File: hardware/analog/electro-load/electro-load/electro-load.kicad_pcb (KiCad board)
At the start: 2 copper layers, 178 x 119 mm, 140 parts, among them J1 AVR-ISP-10, J2 Conn_WallSocket_Earth, J3 INPUT, J4 INPUT, K1 SANYOU_SRD_Form_C, M1 Noctua NF-A14 5V, Q1 2N2222A, Q2 2N2222A, Q3 IPP037N06L3, Q4 IPP037N06L3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

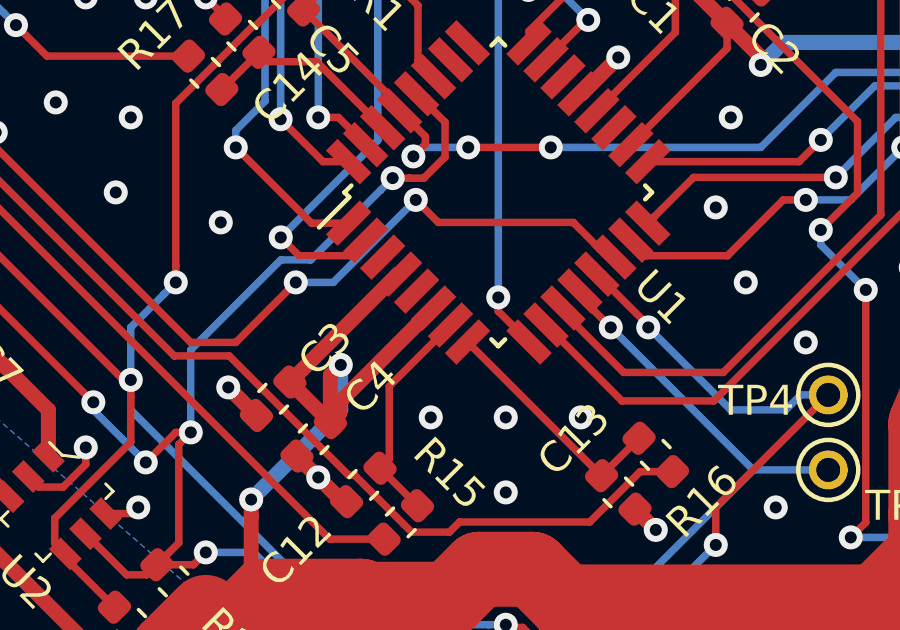
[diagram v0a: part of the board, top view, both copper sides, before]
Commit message: Fixed missing GND trace on SAMD21
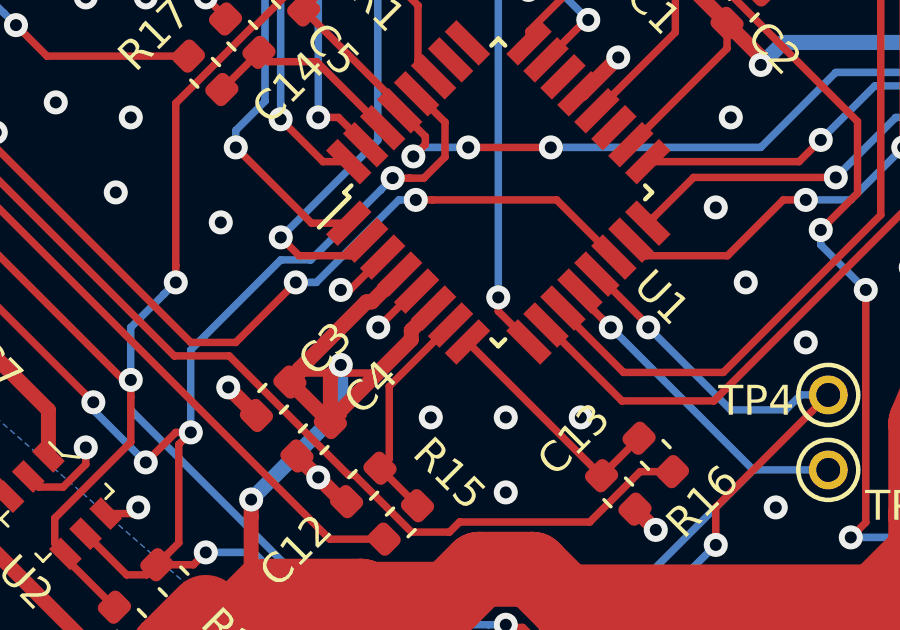
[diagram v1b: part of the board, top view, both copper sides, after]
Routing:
- net GND: track 60.5 -> 64.1 mm, vias 494 -> 496
- net +5V: track 738.6 -> 736.1 mm
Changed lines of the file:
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@@
     (thickness 1.6)
     (drawings 48)
-    (tracks 2043)
+    (tracks 2053)
     (zones 0)
     (modules 140)
@@
     (solder_mask_min_width 0.25)
     (aux_axis_origin 0 0)
-    (visible_elements 7FF5FF7F)
+    (visible_elements 7FFDFF7F)
     (pcbplotparams
       (layerselection 0x010fc_ffffffff)
@@
   (via (at 176 87) (size 0.8) (drill 0.4) (layers F.Cu B.Cu) (net 1))
   (via (at 173.5 89.5) (size 0.8) (drill 0.4) (layers F.Cu B.Cu) (net 1))
+  (segment (start 196.961953 50.788047) (end 195.75 52) (width 0.25) (layer F.Cu) (net 1))
+  (segment (start 197.027639 50.788047) (end 196.961953 50.788047) (width 0.25) (layer F.Cu) (net 1))
+  (via (at 195.75 52) (size 0.8) (drill 0.4) (layers F.Cu B.Cu) (net 1))
+  (segment (start 194.802944 50.75) (end 194.5 50.75) (width 0.25) (layer F.Cu) (net 1))
+  (via (at 194.5 50.75) (size 0.8) (drill 0.4) (layers F.Cu B.Cu) (net 1))
+  (segment (start 195.896268 49.656676) (end 194.802944 50.75) (width 0.25) (layer F.Cu) (net 1))
   (segment (start 188.405065 62.103117) (end 189.483403 61.024779) (width 0.2) (layer F.Cu) (net 2))
   (segment (start 188.069189 62.438993) (end 188.405065 62.103117) (width 0.2) (layer F.Cu) (net 2))
@@
   (segment (start 172.3125 109.065354) (end 172.297854 109.08) (width 0.5) (layer F.Cu) (net 2))
   (segment (start 172.3125 106.95) (end 172.3125 109.065354) (width 0.5) (layer F.Cu) (net 2))
-  (segment (start 196.349711 50.222361) (end 196.461953 50.222361) (width 0.25) (layer F.Cu) (net 2))
-  (segment (start 193.052803 53.519269) (end 196.349711 50.222361) (width 0.25) (layer F.Cu) (net 2))
-  (segment (start 193.052803 54.071283) (end 193.052803 53.519269) (width 0.25) (layer F.Cu) (net 2))
-  (segment (start 194.403377 54.543679) (end 194.403377 55.421857) (width 0.25) (layer F.Cu) (net 2))
-  (segment (start 197.593324 51.353732) (end 194.403377 54.543679) (width 0.25) (layer F.Cu) (net 2))
-  (segment (start 194.403377 55.421857) (end 193.052803 54.071283) (width 0.25) (layer F.Cu) (net 2))
   (segment (start 205.651881 42.163805) (end 203.038047 44.777639) (width 0.25) (layer F.Cu) (net 2))
   (segment (start 205.651881 40.759262) (end 205.651881 42.163805) (width 0.25) (layer F.Cu) (net 2))
@@
   (segment (start 181.174898 56.181098) (end 181.952716 56.181098) (width 0.5) (layer F.Cu) (net 2))
   (segment (start 188.75 64.25) (end 188.75 62.75) (width 2.5) (layer F.Cu) (net 2))
-  (segment (start 194.462736 54.48432) (end 197.593324 51.353732) (width 0.5) (layer F.Cu) (net 2))
-  (segment (start 194.462736 54.862498) (end 194.462736 54.48432) (width 0.5) (layer F.Cu) (net 2))
-  (segment (start 194.153377 55.171857) (end 194.462736 54.862498) (width 0.5) (layer F.Cu) (net 2))
-  (segment (start 196.401725 50.222361) (end 192.802803 53.821283) (width 0.5) (layer F.Cu) (net 2))
-  (segment (start 196.461953 50.222361) (end 196.401725 50.222361) (width 0.5) (layer F.Cu) (net 2))
   (segment (start 194.153377 55.171857) (end 192.802803 53.821283) (width 0.5) (layer F.Cu) (net 2))
   (via (at 194.5 53.25) (size 0.8) (drill 0.4) (layers F.Cu B.Cu) (net 2))
@@
   (segment (start 194.5 82.46) (end 197.55 79.41) (width 0.5) (layer F.Cu) (net 2))
   (segment (start 197.55 79.41) (end 198.6275 79.41) (width 0.5) (layer F.Cu) (net 2))
+  (segment (start 196.850002 52.097054) (end 197.593324 51.353732) (width 0.5) (layer F.Cu) (net 2))
+  (segment (start 197.593324 51.47968) (end 195.553735 53.519269) (width 0.25) (layer F.Cu) (net 2))
+  (segment (start 197.593324 51.353732) (end 197.593324 51.47968) (width 0.25) (layer F.Cu) (net 2))
+  (segment (start 195.553735 53.519269) (end 193.165045 53.519269) (width 0.25) (layer F.Cu) (net 2))
+  (segment (start 194.462736 54.795268) (end 196.850002 52.408002) (width 0.5) (layer F.Cu) (net 2))
+  (segment (start 194.462736 54.862498) (end 194.462736 54.795268) (width 0.5) (layer F.Cu) (net 2))
+  (segment (start 193.165045 53.519269) (end 196.461953 50.222361) (width 0.25) (layer F.Cu) (net 2))
+  (segment (start 196.850002 52.408002) (end 196.850002 52.097054) (width 0.5) (layer F.Cu) (net 2))
+  (segment (start 194.153377 55.171857) (end 194.462736 54.862498) (width 0.5) (layer F.Cu) (net 2))
+  (segment (start 195.350002 51.149998) (end 193.112162 53.387838) (width 0.5) (layer F.Cu) (net 2))
+  (segment (start 193.112162 53.387838) (end 193.112162 53.511924) (width 0.5) (layer F.Cu) (net 2))
+  (segment (start 195.534316 51.149998) (end 195.350002 51.149998) (width 0.5) (layer F.Cu) (net 2))
+  (segment (start 196.461953 50.222361) (end 195.534316 51.149998) (width 0.5) (layer F.Cu) (net 2))
+  (segment (start 193.112162 53.511924) (end 192.802803 53.821283) (width 0.5) (layer F.Cu) (net 2))
   (segment (start 193.60057 41.082554) (end 194.678908 40.004216) (width 0.2) (layer F.Cu) (net 3))
   (segment (start 193.264694 41.41843) (end 193.60057 41.082554) (width 0.2) (layer F.Cu) (net 3))
@@
   (segment (start 119.75 39.8375) (end 119.5 39.5875) (width 0.2) (layer F.Cu) (net 19))
   (segment (start 119.75 43.55) (end 119.75 39.8375) (width 0.2) (layer F.Cu) (net 19))
-  (segment (start 194.25 50.5) (end 193 50.5) (width 0.25) (layer B.Cu) (net 19))
-  (segment (start 203.603732 49.656676) (end 203.406676 49.656676) (width 0.25) (layer F.Cu) (net 19))
-  (segment (start 197.75 48.5) (end 197 47.75) (width 0.25) (layer F.Cu) (net 19))
-  (segment (start 203.406676 49.656676) (end 202.25 48.5) (width 0.25) (layer F.Cu) (net 19))
-  (segment (start 202.25 48.5) (end 197.75 48.5) (width 0.25) (layer F.Cu) (net 19))
-  (segment (start 197 47.75) (end 194.25 50.5) (width 0.25) (layer B.Cu) (net 19))
   (via (at 193 50.5) (size 0.8) (drill 0.4) (layers F.Cu B.Cu) (net 19))
   (via (at 197 47.75) (size 0.8) (drill 0.4) (layers F.Cu B.Cu) (net 19))
@@
   (segment (start 183 46) (end 183 45.5) (width 0.25) (layer F.Cu) (net 19))
   (segment (start 189.5 52.5) (end 183 46) (width 0.25) (layer F.Cu) (net 19))
+  (segment (start 203.603732 49.656676) (end 201.697056 47.75) (width 0.25) (layer F.Cu) (net 19))
+  (segment (start 197 47.75) (end 196.434315 47.75) (width 0.25) (layer B.Cu) (net 19))
+  (segment (start 201.697056 47.75) (end 197.565685 47.75) (width 0.25) (layer F.Cu) (net 19))
+  (segment (start 193.684315 50.5) (end 193.565685 50.5) (width 0.25) (layer B.Cu) (net 19))
+  (segment (start 197.565685 47.75) (end 197 47.75) (width 0.25) (layer F.Cu) (net 19))
+  (segment (start 196.434315 47.75) (end 193.684315 50.5) (width 0.25) (layer B.Cu) (net 19))
+  (segment (start 193.565685 50.5) (end 193 50.5) (width 0.25) (layer B.Cu) (net 19))
   (via (at 118.75 48.5) (size 0.8) (drill 0.4) (layers F.Cu B.Cu) (net 20))
   (via (at 114.25 48.25) (size 0.8) (drill 0.4) (layers F.Cu B.Cu) (net 20))

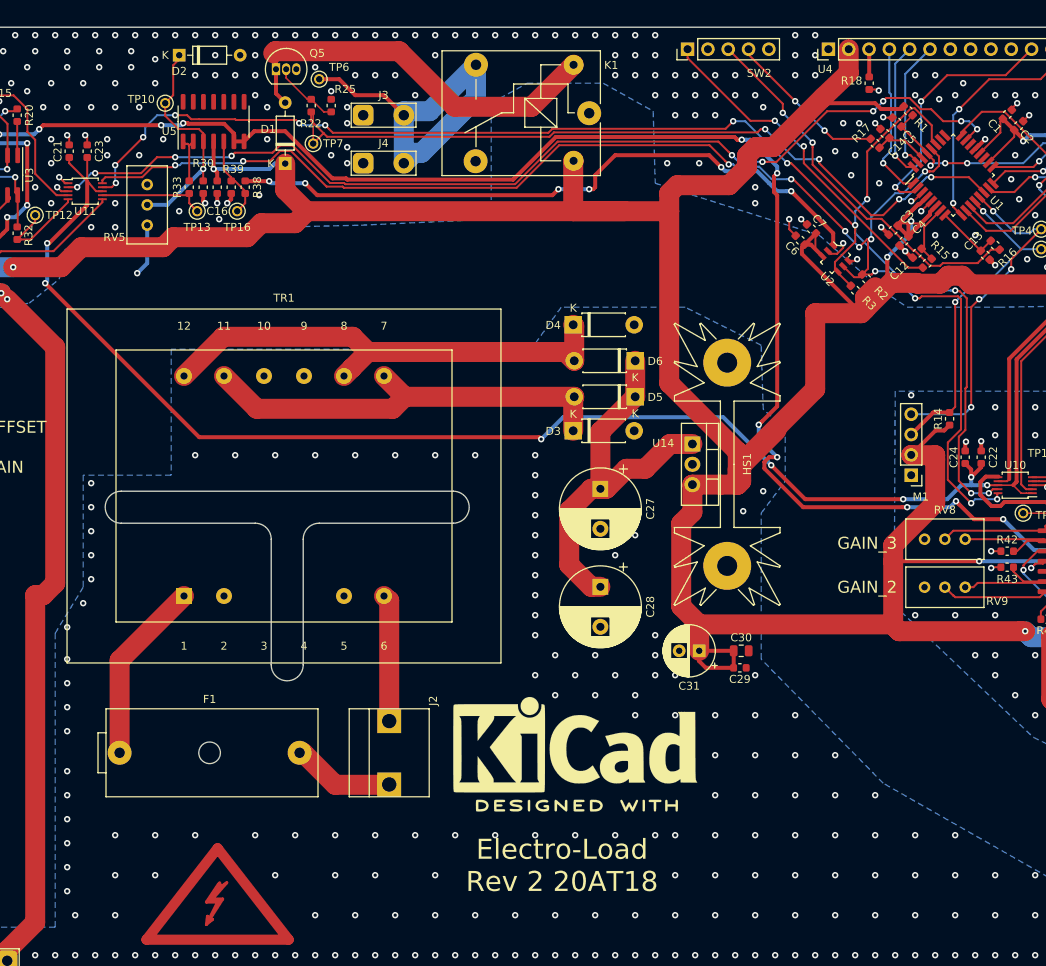
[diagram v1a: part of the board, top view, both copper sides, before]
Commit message: Added mounting holes and added silkscreen text for V_DIV
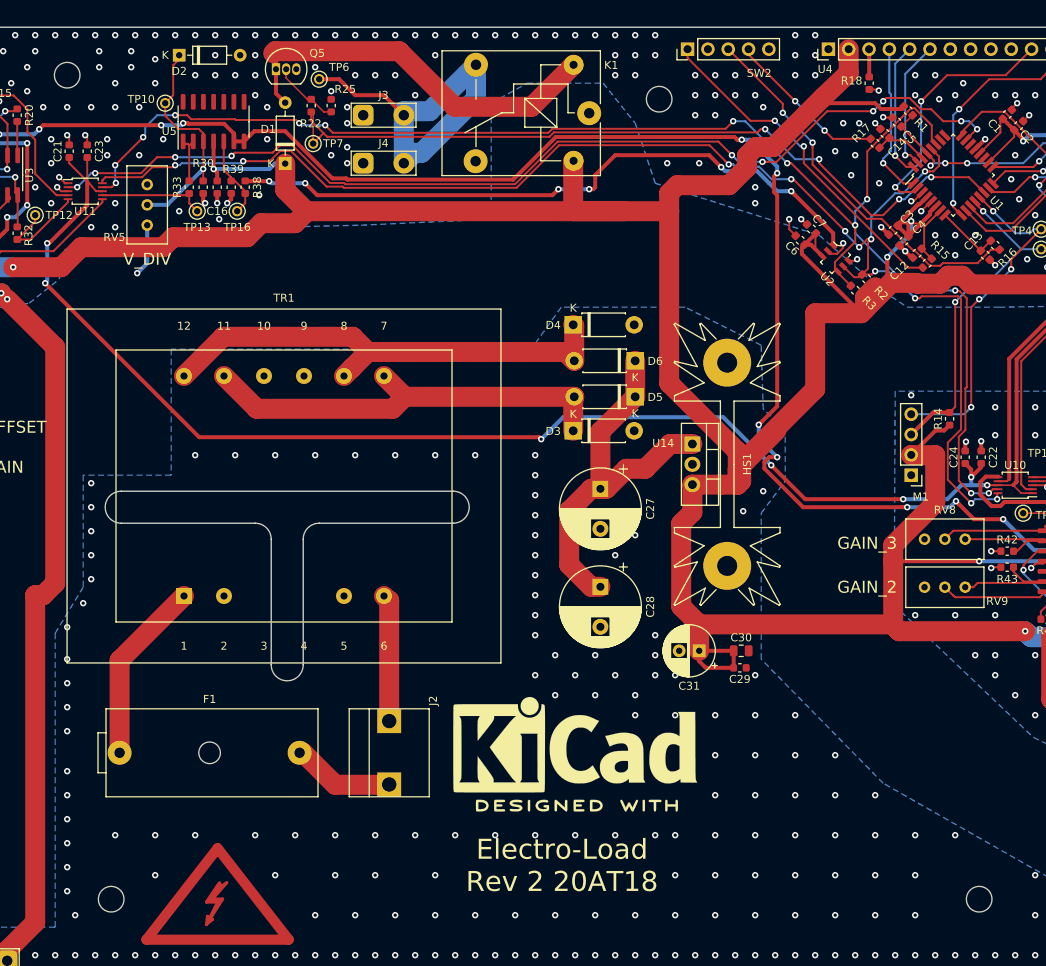
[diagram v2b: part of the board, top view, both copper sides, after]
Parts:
- added REF**: MountingHole_3.2mm_M3, MountingHole:MountingHole_3.2mm_M3, F.Cu at (89.0, 35.0)
- added REF**: MountingHole_3.2mm_M3, MountingHole:MountingHole_3.2mm_M3, F.Cu at (163.0, 38.0)
- added REF**: MountingHole_3.2mm_M3, MountingHole:MountingHole_3.2mm_M3, F.Cu at (203.0, 138.0)
- added REF**: MountingHole_3.2mm_M3, MountingHole:MountingHole_3.2mm_M3, F.Cu at (94.5, 138.0)
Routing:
- net GND: vias 496 -> 481
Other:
- board text added: "V_DIV"
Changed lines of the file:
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@@
   (general
     (thickness 1.6)
-    (drawings 48)
-    (tracks 2053)
+    (drawings 49)
+    (tracks 2038)
     (zones 0)
-    (modules 140)
+    (modules 144)
     (nets 89)
   )
@@
     (add_net "/Current Measurements/LOAD_CURRENT")
   )
+  (module MountingHole:MountingHole_3.2mm_M3 (layer F.Cu)
+    (at 89 35)
+    (descr "Mounting Hole 3.2mm, no annular, M3")
+    (tags "mounting hole 3.2mm no annular m3")
+    (attr virtual)
+    (fp_text reference REF** (at 0 -4.2) (layer F.SilkS) hide
+      (effects (font (size 1 1) (thickness 0.15)))
+    )
+    (fp_text value MountingHole_3.2mm_M3 (at 0 4.2) (layer F.Fab)
+      (effects (font (size 1 1) (thickness 0.15)))
+    )
+    (fp_text user %R (at 0.3 0) (layer F.Fab)
+      (effects (font (size 1 1) (thickness 0.15)))
+    )
+    (fp_circle (center 0 0) (end 3.2 0) (layer Cmts.User) (width 0.15))
+    (fp_circle (center 0 0) (end 3.45 0) (layer F.CrtYd) (width 0.05))
+    (pad 1 np_thru_hole circle (at 0 0) (size 3.2 3.2) (drill 3.2) (layers *.Cu *.Mask))
+  )
+  (module MountingHole:MountingHole_3.2mm_M3 (layer F.Cu)
+    (at 163 38)
+    (descr "Mounting Hole 3.2mm, no annular, M3")
+    (tags "mounting hole 3.2mm no annular m3")
+    (attr virtual)
+    (fp_text reference REF** (at 0 -4.2) (layer F.SilkS) hide
+      (effects (font (size 1 1) (thickness 0.15)))
+    )
+    (fp_text value MountingHole_3.2mm_M3 (at 0 4.2) (layer F.Fab)
+      (effects (font (size 1 1) (thickness 0.15)))
+    )
+    (fp_circle (center 0 0) (end 3.45 0) (layer F.CrtYd) (width 0.05))
+    (fp_circle (center 0 0) (end 3.2 0) (layer Cmts.User) (width 0.15))
+    (fp_text user %R (at 0.3 0) (layer F.Fab)
+      (effects (font (size 1 1) (thickness 0.15)))
+    )
+    (pad 1 np_thru_hole circle (at 0 0) (size 3.2 3.2) (drill 3.2) (layers *.Cu *.Mask))
+  )
+  (module MountingHole:MountingHole_3.2mm_M3 (layer F.Cu)
+    (at 203 138)
+    (descr "Mounting Hole 3.2mm, no annular, M3")
+    (tags "mounting hole 3.2mm no annular m3")
+    (attr virtual)
+    (fp_text reference REF** (at 0 -4.2) (layer F.SilkS) hide
+      (effects (font (size 1 1) (thickness 0.15)))
+    )
+    (fp_text value MountingHole_3.2mm_M3 (at 0 4.2) (layer F.Fab)
+      (effects (font (size 1 1) (thickness 0.15)))
+    )
+    (fp_text user %R (at 0.3 0) (layer F.Fab)
+      (effects (font (size 1 1) (thickness 0.15)))
+    )
+    (fp_circle (center 0 0) (end 3.2 0) (layer Cmts.User) (width 0.15))
+    (fp_circle (center 0 0) (end 3.45 0) (layer F.CrtYd) (width 0.05))
+    (pad 1 np_thru_hole circle (at 0 0) (size 3.2 3.2) (drill 3.2) (layers *.Cu *.Mask))
+  )
+  (module MountingHole:MountingHole_3.2mm_M3 (layer F.Cu)
+    (at 94.5 138)
+    (descr "Mounting Hole 3.2mm, no annular, M3")
+    (tags "mounting hole 3.2mm no annular m3")
+    (attr virtual)
+    (fp_text reference REF** (at 0 -4.2) (layer F.SilkS) hide
+      (effects (font (size 1 1) (thickness 0.15)))
+    )
+    (fp_text value MountingHole_3.2mm_M3 (at 0 4.2) (layer F.Fab)
+      (effects (font (size 1 1) (thickness 0.15)))
+    )
+    (fp_circle (center 0 0) (end 3.45 0) (layer F.CrtYd) (width 0.05))
+    (fp_circle (center 0 0) (end 3.2 0) (layer Cmts.User) (width 0.15))
+    (fp_text user %R (at 0.3 0) (layer F.Fab)
+      (effects (font (size 1 1) (thickness 0.15)))
+    )
+    (pad 1 np_thru_hole circle (at 0 0) (size 3.2 3.2) (drill 3.2) (layers *.Cu *.Mask))
+  )
   (module Button_Switch_THT:SW_PUSH_6mm_H4.3mm (layer F.Cu)
     (at 232 57 90)
@@
     )
   )
+  (gr_text V_DIV (at 99 58) (layer F.SilkS)
+    (effects (font (size 1.5 1.5) (thickness 0.15)))
+  )
   (gr_text GAIN_2 (at 189 99) (layer F.SilkS)
     (effects (font (size 1.5 1.5) (thickness 0.15)))
@@
   (via (at 77.5 142.5) (size 0.8) (drill 0.4) (layers F.Cu B.Cu) (net 1))
   (via (at 90 140) (size 0.8) (drill 0.4) (layers F.Cu B.Cu) (net 1))
-  (via (at 95 140) (size 0.8) (drill 0.4) (layers F.Cu B.Cu) (net 1))
   (via (at 100 135) (size 0.8) (drill 0.4) (layers F.Cu B.Cu) (net 1))
-  (via (at 95 135) (size 0.8) (drill 0.4) (layers F.Cu B.Cu) (net 1))
   (via (at 89 128) (size 0.8) (drill 0.4) (layers F.Cu B.Cu) (net 1))
   (via (at 89 125) (size 0.8) (drill 0.4) (layers F.Cu B.Cu) (net 1))
@@
   (via (at 190 140) (size 0.8) (drill 0.4) (layers F.Cu B.Cu) (net 1))
   (via (at 195 140) (size 0.8) (drill 0.4) (layers F.Cu B.Cu) (net 1))
-  (via (at 200 140) (size 0.8) (drill 0.4) (layers F.Cu B.Cu) (net 1))
-  (via (at 205 140) (size 0.8) (drill 0.4) (layers F.Cu B.Cu) (net 1))
   (via (at 210 140) (size 0.8) (drill 0.4) (layers F.Cu B.Cu) (net 1))
   (via (at 215 140) (size 0.8) (drill 0.4) (layers F.Cu B.Cu) (net 1))
   (via (at 210 135) (size 0.8) (drill 0.4) (layers F.Cu B.Cu) (net 1))
-  (via (at 205 135) (size 0.8) (drill 0.4) (layers F.Cu B.Cu) (net 1))
   (via (at 200 130) (size 0.8) (drill 0.4) (layers F.Cu B.Cu) (net 1))
-  (via (at 200 135) (size 0.8) (drill 0.4) (layers F.Cu B.Cu) (net 1))
   (via (at 195 130) (size 0.8) (drill 0.4) (layers F.Cu B.Cu) (net 1))
   (via (at 190 125) (size 0.8) (drill 0.4) (layers F.Cu B.Cu) (net 1))
@@
   (via (at 176 39) (size 0.8) (drill 0.4) (layers F.Cu B.Cu) (net 1))
   (via (at 170 40) (size 0.8) (drill 0.4) (layers F.Cu B.Cu) (net 1))
-  (via (at 167.5 40) (size 0.8) (drill 0.4) (layers F.Cu B.Cu) (net 1))
-  (via (at 165 40) (size 0.8) (drill 0.4) (layers F.Cu B.Cu) (net 1))
-  (via (at 162.5 37.5) (size 0.8) (drill 0.4) (layers F.Cu B.Cu) (net 1))
   (via (at 157.5 35) (size 0.8) (drill 0.4) (layers F.Cu B.Cu) (net 1))
   (via (at 160 35) (size 0.8) (drill 0.4) (layers F.Cu B.Cu) (net 1))
-  (via (at 165 37.5) (size 0.8) (drill 0.4) (layers F.Cu B.Cu) (net 1))
   (via (at 167.5 37.5) (size 0.8) (drill 0.4) (layers F.Cu B.Cu) (net 1))
   (via (at 170 37.5) (size 0.8) (drill 0.4) (layers F.Cu B.Cu) (net 1))
   (via (at 167.5 35) (size 0.8) (drill 0.4) (layers F.Cu B.Cu) (net 1))
-  (via (at 165 35) (size 0.8) (drill 0.4) (layers F.Cu B.Cu) (net 1))
-  (via (at 162.5 35) (size 0.8) (drill 0.4) (layers F.Cu B.Cu) (net 1))
   (via (at 162.5 32.5) (size 0.8) (drill 0.4) (layers F.Cu B.Cu) (net 1))
   (via (at 162.5 30) (size 0.8) (drill 0.4) (layers F.Cu B.Cu) (net 1))
@@
   (via (at 81 32) (size 0.8) (drill 0.4) (layers F.Cu B.Cu) (net 1))
   (via (at 85 32) (size 0.8) (drill 0.4) (layers F.Cu B.Cu) (net 1))
-  (via (at 89 32) (size 0.8) (drill 0.4) (layers F.Cu B.Cu) (net 1))
   (via (at 93 32) (size 0.8) (drill 0.4) (layers F.Cu B.Cu) (net 1))
   (via (at 97 32) (size 0.8) (drill 0.4) (layers F.Cu B.Cu) (net 1))
@@
   (via (at 80 34) (size 0.8) (drill 0.4) (layers F.Cu B.Cu) (net 1))
   (via (at 84 34) (size 0.8) (drill 0.4) (layers F.Cu B.Cu) (net 1))
-  (via (at 87 36) (size 0.8) (drill 0.4) (layers F.Cu B.Cu) (net 1))
-  (via (at 91 36) (size 0.8) (drill 0.4) (layers F.Cu B.Cu) (net 1))
   (via (at 95 36) (size 0.8) (drill 0.4) (layers F.Cu B.Cu) (net 1))
   (via (at 97 34) (size 0.8) (drill 0.4) (layers F.Cu B.Cu) (net 1))
   (via (at 93 34) (size 0.8) (drill 0.4) (layers F.Cu B.Cu) (net 1))
-  (via (at 89 34) (size 0.8) (drill 0.4) (layers F.Cu B.Cu) (net 1))
   (via (at 94 43) (size 0.8) (drill 0.4) (layers F.Cu B.Cu) (net 1))
   (via (at 94 45) (size 0.8) (drill 0.4) (layers F.Cu B.Cu) (net 1))
@@
   (via (at 194.5 50.75) (size 0.8) (drill 0.4) (layers F.Cu B.Cu) (net 1))
   (segment (start 195.896268 49.656676) (end 194.802944 50.75) (width 0.25) (layer F.Cu) (net 1))
+  (via (at 167.5 40) (size 0.8) (drill 0.4) (layers F.Cu B.Cu) (net 1))
   (segment (start 188.405065 62.103117) (end 189.483403 61.024779) (width 0.2) (layer F.Cu) (net 2))
   (segment (start 188.069189 62.438993) (end 188.405065 62.103117) (width 0.2) (layer F.Cu) (net 2))
@@
     (polygon
       (pts
-        (xy 162.25 39.5) (xy 162.5 48.5) (xy 183 55) (xy 191 62) (xy 194 64)
+        (xy 160 41) (xy 162.5 48.5) (xy 183 55) (xy 191 62) (xy 194 64)
         (xy 205.5 64) (xy 236.6 63.5) (xy 236.6 65) (xy 237.3 65.5) (xy 240.25 65.5)
         (xy 240.25 68) (xy 237.3 68) (xy 236.5 68.9) (xy 236.5 71.5) (xy 234.5 74.5)
